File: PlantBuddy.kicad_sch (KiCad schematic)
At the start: 75 parts, among them J1 USB_C_Receptacle_USB2.0, J101 JST, J102 Debug, J4 External, SW1 SW_Push, U1 LTR-303ALS-01, U101 AP2139AK-3.0TRG1, U102 nRF52832-QFAA, U104 XB5350A, U105 CN809T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

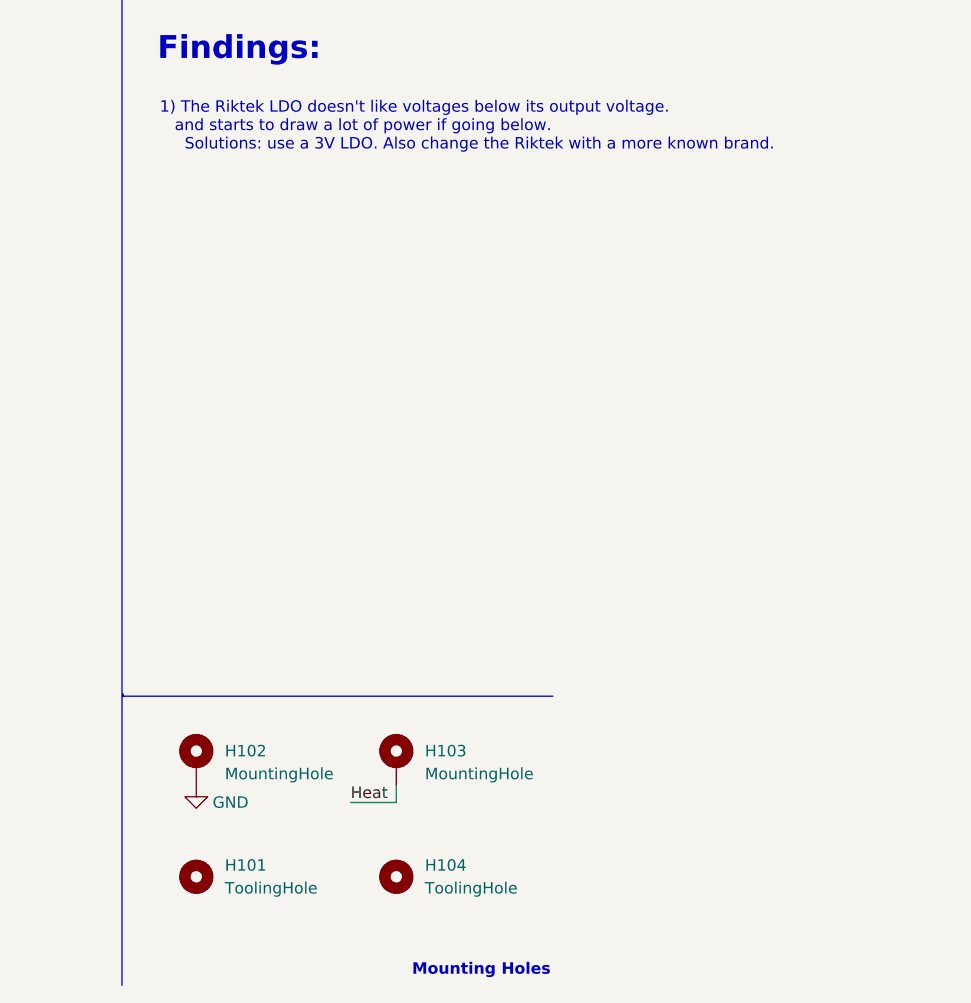
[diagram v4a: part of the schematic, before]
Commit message: Changed antenna configuration back.
After testing I found out that this antenna configuration works
better.
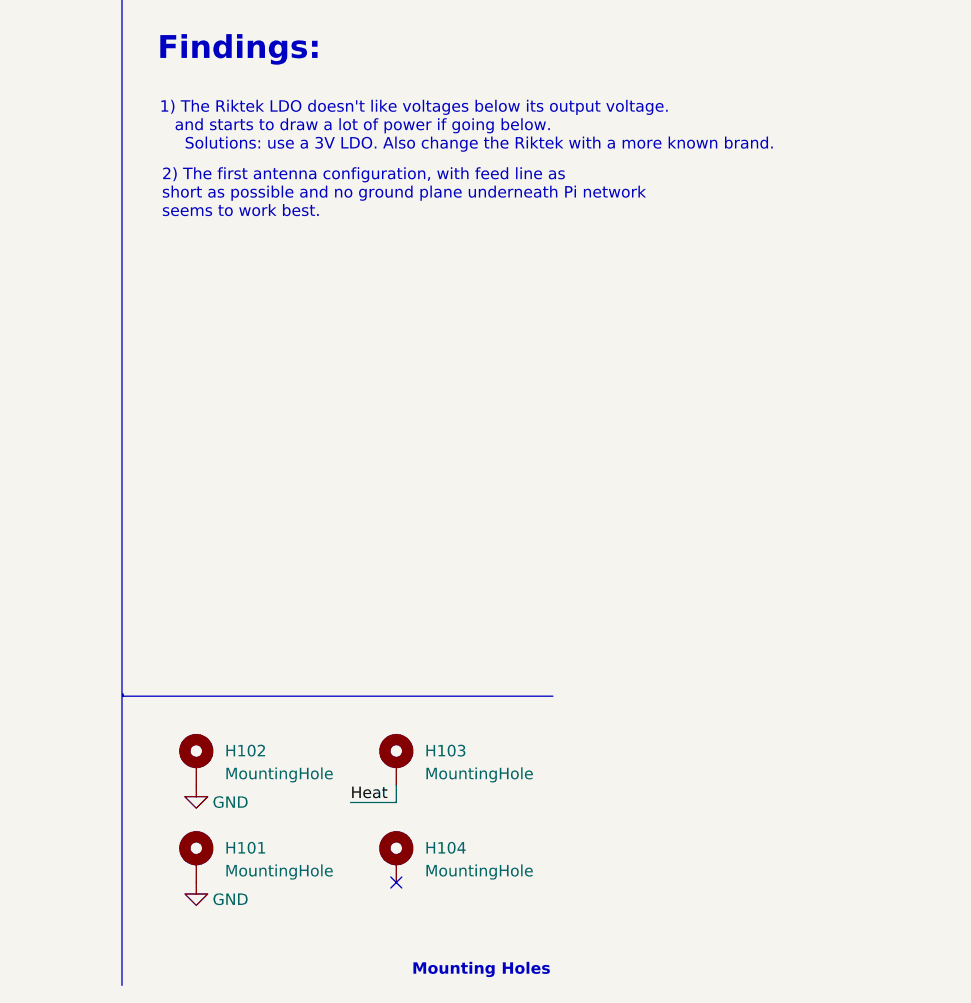
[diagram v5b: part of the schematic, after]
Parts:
- removed H101, H104: ToolingHole, Tooling:JLCPCB_Tooling_hole, symbol Mechanical:MountingHole
- added H101, H104: MountingHole, MountingHole:MountingHole_2.2mm_M2_DIN965_Pad, symbol Mechanical:MountingHole_Pad
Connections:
- net GND: now also H101.1
- no-connect marks 25 -> 26
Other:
- note added: "2) The first antenna configuration, with feed line as short as possible and no ground plane underneath Pi network seems to work best."
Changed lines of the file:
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@@
   (no_connect (at 276.225 143.51))
   (no_connect (at 245.745 37.465))
+  (no_connect (at 282.575 273.685))
   (no_connect (at 42.545 52.07))
   (no_connect (at 42.545 49.53))
@@
     (effects (font (size 1.27 1.27) bold) (justify right bottom))
   )
+  (text "2) The first antenna configuration, with feed line as\nshort as possible and no ground plane underneath Pi network\nseems to work best."
+    (at 256.54 200.025 0)
+    (effects (font (size 1.27 1.27)) (justify left bottom))
+  )
   (text "<- Main Supply Voltage" (at 313.182 29.845 180)
     (effects (font (size 1.27 1.27) bold) (justify right bottom))
@@
     (pin "3")
   )
-  (symbol (lib_id "Mechanical:MountingHole") (at 282.575 273.05 0) (unit 1)
-    (in_bom yes) (on_board yes) (fields_autoplaced)
-    (property "Reference" "H104" (id 0) (at 285.75 271.7799 0)
-      (effects (font (size 1.27 1.27)) (justify left))
-    )
-    (property "Value" "ToolingHole" (id 1) (at 285.75 274.3199 0)
-      (effects (font (size 1.27 1.27)) (justify left))
-    )
-    (property "Footprint" "Tooling:JLCPCB_Tooling_hole" (id 2) (at 282.575 273.05 0)
-      (effects (font (size 1.27 1.27)) hide)
-    )
-    (property "Datasheet" "~" (id 3) (at 282.575 273.05 0)
-      (effects (font (size 1.27 1.27)) hide)
-    )
-  )
   (symbol (lib_id "Connector:TestPoint_Small") (at 397.51 31.75 0) (unit 1)
     (in_bom yes) (on_board yes)
@@
     (pin "2")
   )
+  (symbol (lib_id "PlantBuddy-rescue:GND-power") (at 260.35 273.685 0) (mirror y) (unit 1)
+    (in_bom yes) (on_board yes)
+    (property "Reference" "#PWR0121" (id 0) (at 260.35 280.035 0)
+      (effects (font (size 1.27 1.27)) hide)
+    )
+    (property "Value" "GND" (id 1) (at 264.16 275.59 0))
+    (property "Footprint" "" (id 2) (at 260.35 273.685 0)
+      (effects (font (size 1.27 1.27)) hide)
+    )
+    (property "Datasheet" "" (id 3) (at 260.35 273.685 0)
+      (effects (font (size 1.27 1.27)) hide)
+    )
+    (pin "1")
+  )
   (symbol (lib_id "PlantBuddy-rescue:GND-power") (at 147.955 154.94 0) (mirror y) (unit 1)
     (in_bom yes) (on_board yes)
@@
     (pin "2")
   )
+  (symbol (lib_id "Mechanical:MountingHole_Pad") (at 282.575 271.145 0) (unit 1)
+    (in_bom yes) (on_board yes) (fields_autoplaced)
+    (property "Reference" "H104" (id 0) (at 285.75 269.8749 0)
+      (effects (font (size 1.27 1.27)) (justify left))
+    )
+    (property "Value" "MountingHole" (id 1) (at 285.75 272.4149 0)
+      (effects (font (size 1.27 1.27)) (justify left))
+    )
+    (property "Footprint" "MountingHole:MountingHole_2.2mm_M2_DIN965_Pad" (id 2) (at 282.575 271.145 0)
+      (effects (font (size 1.27 1.27)) hide)
+    )
+    (property "Datasheet" "~" (id 3) (at 282.575 271.145 0)
+      (effects (font (size 1.27 1.27)) hide)
+    )
+    (pin "1")
+  )
   (symbol (lib_id "Device:R_Small") (at 321.945 103.505 180) (unit 1)
     (in_bom yes) (on_board yes)
@@
     (pin "1")
   )
-  (symbol (lib_id "Mechanical:MountingHole") (at 260.35 273.05 0) (unit 1)
-    (in_bom yes) (on_board yes) (fields_autoplaced)
-    (property "Reference" "H101" (id 0) (at 263.525 271.7799 0)
-      (effects (font (size 1.27 1.27)) (justify left))
-    )
-    (property "Value" "ToolingHole" (id 1) (at 263.525 274.3199 0)
-      (effects (font (size 1.27 1.27)) (justify left))
-    )
-    (property "Footprint" "Tooling:JLCPCB_Tooling_hole" (id 2) (at 260.35 273.05 0)
-      (effects (font (size 1.27 1.27)) hide)
-    )
-    (property "Datasheet" "~" (id 3) (at 260.35 273.05 0)
-      (effects (font (size 1.27 1.27)) hide)
-    )
-  )
   (symbol (lib_id "Device:C_Small") (at 255.27 68.58 0) (unit 1)
     (in_bom yes) (on_board yes) (fields_autoplaced)
@@
     (pin "1")
   )
+  (symbol (lib_id "Mechanical:MountingHole_Pad") (at 260.35 271.145 0) (unit 1)
+    (in_bom yes) (on_board yes) (fields_autoplaced)
+    (property "Reference" "H101" (id 0) (at 263.525 269.8749 0)
+      (effects (font (size 1.27 1.27)) (justify left))
+    )
+    (property "Value" "MountingHole" (id 1) (at 263.525 272.4149 0)
+      (effects (font (size 1.27 1.27)) (justify left))
+    )
+    (property "Footprint" "MountingHole:MountingHole_2.2mm_M2_DIN965_Pad" (id 2) (at 260.35 271.145 0)
+      (effects (font (size 1.27 1.27)) hide)
+    )
+    (property "Datasheet" "~" (id 3) (at 260.35 271.145 0)
+      (effects (font (size 1.27 1.27)) hide)
+    )
+    (pin "1")
+  )
   (symbol (lib_id "Battery_Management:BQ24072RGT") (at 258.445 40.005 0) (unit 1)
     (in_bom yes) (on_board yes)
@@
       (reference "#PWR0120") (unit 1) (value "+3V0") (footprint "")
     )
+    (path "/5780cd04-1c91-4153-83dc-43d54dc326b0"
+      (reference "#PWR0121") (unit 1) (value "GND") (footprint "")
+    )
     (path "/36f1eb4a-d699-4504-a771-be3e978b3a9a"
       (reference "#PWR0122") (unit 1) (value "GND") (footprint "")
@@
       (reference "D102") (unit 1) (value "LED_RGBA") (footprint "LED_SMD:LED_Lumex_SML-LX0404SIUPGUSB")
     )
-    (path "/8111a967-c093-491f-97fe-4178a7b81b23"
-      (reference "H101") (unit 1) (value "ToolingHole") (footprint "Tooling:JLCPCB_Tooling_hole")
+    (path "/dc462337-939a-4960-b4a0-904cbdb3d7e2"
+      (reference "H101") (unit 1) (value "MountingHole") (footprint "MountingHole:MountingHole_2.2mm_M2_DIN965_Pad")
     )
     (path "/8ab94929-ad36-4747-8cd3-d4e063f12079"
@@
       (reference "H103") (unit 1) (value "MountingHole") (footprint "MountingHole:MountingHole_2.2mm_M2_DIN965_Pad")
     )
-    (path "/1b909cb5-2d26-4c06-b8a7-78dae45bfa2b"
-      (reference "H104") (unit 1) (value "ToolingHole") (footprint "Tooling:JLCPCB_Tooling_hole")
+    (path "/643da22a-c92b-49e7-b814-6ea6b4f90faa"
+      (reference "H104") (unit 1) (value "MountingHole") (footprint "MountingHole:MountingHole_2.2mm_M2_DIN965_Pad")
     )
     (path "/4138c96d-aa03-4df3-a048-35a223d1d760"

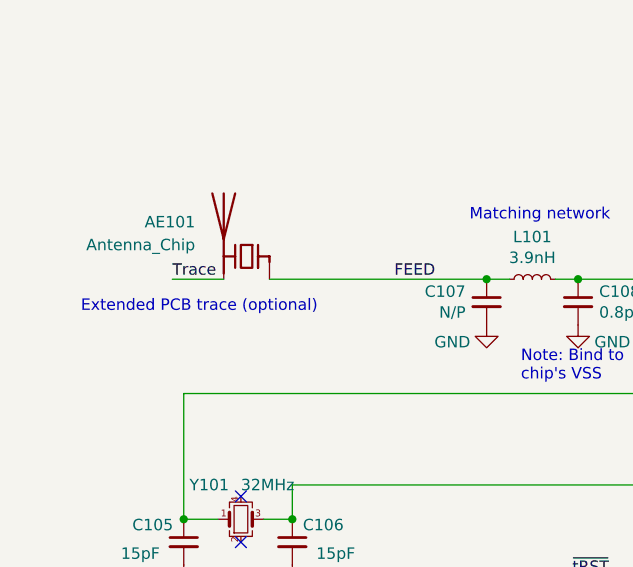
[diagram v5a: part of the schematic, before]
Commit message: Changed to IFA antenna
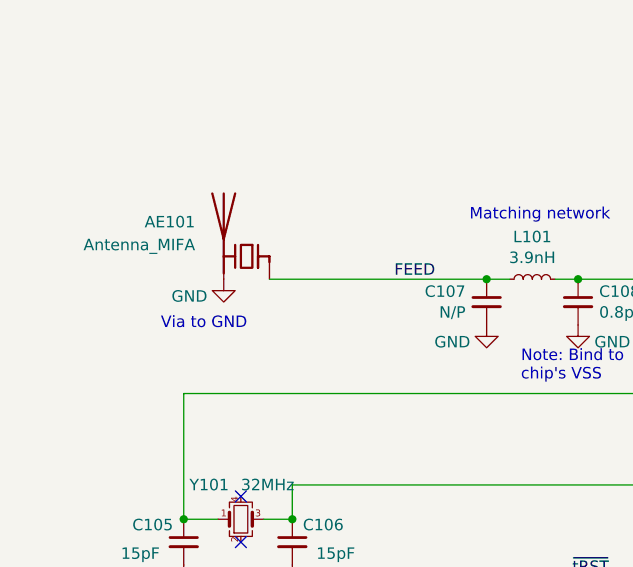
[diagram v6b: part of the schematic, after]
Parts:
- AE101: value Antenna_Chip -> Antenna_MIFA; footprint LED_SMD:LED_1206_3216Metric -> RF_Antenna:Texas_SWRA117D_2.4GHz_Left
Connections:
- net Trace is gone; now on net GND: AE101.2 (PCB_Trace)
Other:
- note added: "Via to GND"
- note removed: "Extended PCB trace (optional)"
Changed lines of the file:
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@@
     (stroke (width 0) (type default) (color 0 0 0 0))
   )
-  (wire (pts (xy 34.925 180.975) (xy 29.21 180.975))
-    (stroke (width 0) (type default) (color 0 0 0 0))
-  )
   (wire (pts (xy 127.635 198.755) (xy 138.43 198.755))
     (stroke (width 0) (type default) (color 0 0 0 0))
@@
     (effects (font (size 1.27 1.27)) (justify left bottom))
   )
-  (text "Extended PCB trace (optional)\n" (at 19.05 184.785 0)
+  (text "Via to GND" (at 27.94 186.69 0)
     (effects (font (size 1.27 1.27)) (justify left bottom))
   )
@@
     (effects (font (size 1.27 1.27)) (justify right bottom))
   )
-  (label "Trace" (at 29.21 180.975 0)
-    (effects (font (size 1.27 1.27)) (justify left bottom))
-  )
   (label "SCL" (at 318.135 108.585 0)
     (effects (font (size 1.27 1.27)) (justify left bottom))
@@
       (effects (font (size 1.27 1.27)) (justify left))
     )
-    (property "Value" "Antenna_Chip" (id 1) (at 31.75 177.1649 0)
+    (property "Value" "Antenna_MIFA" (id 1) (at 31.75 177.1649 0)
       (effects (font (size 1.27 1.27)) (justify left))
     )
-    (property "Footprint" "LED_SMD:LED_1206_3216Metric" (id 2) (at 40.005 173.99 0)
+    (property "Footprint" "RF_Antenna:Texas_SWRA117D_2.4GHz_Left" (id 2) (at 40.005 173.99 0)
       (effects (font (size 1.27 1.27)) hide)
     )
@@
     (pin "1")
   )
+  (symbol (lib_id "PlantBuddy-rescue:GND-power") (at 34.925 180.975 0) (unit 1)
+    (in_bom yes) (on_board yes)
+    (property "Reference" "#PWR?" (id 0) (at 34.925 187.325 0)
+      (effects (font (size 1.27 1.27)) hide)
+    )
+    (property "Value" "GND" (id 1) (at 31.115 182.88 0))
+    (property "Footprint" "" (id 2) (at 34.925 180.975 0)
+      (effects (font (size 1.27 1.27)) hide)
+    )
+    (property "Datasheet" "" (id 3) (at 34.925 180.975 0)
+      (effects (font (size 1.27 1.27)) hide)
+    )
+    (pin "1")
+  )
   (symbol (lib_id "power:VCC") (at 361.188 73.025 0) (unit 1)
     (in_bom yes) (on_board yes) (fields_autoplaced)
@@
       (reference "#PWR0135") (unit 1) (value "GND") (footprint "")
     )
+    (path "/a80f6003-26ac-4b9c-a6ac-c9d4176d44bc"
+      (reference "#PWR?") (unit 1) (value "GND") (footprint "")
+    )
     (path "/400ec827-23d4-4dc8-9011-0b8d912989c5"
-      (reference "AE101") (unit 1) (value "Antenna_Chip") (footprint "LED_SMD:LED_1206_3216Metric")
+      (reference "AE101") (unit 1) (value "Antenna_MIFA") (footprint "RF_Antenna:Texas_SWRA117D_2.4GHz_Left")
     )
     (path "/00000000-0000-0000-0000-00005fc5077f"
